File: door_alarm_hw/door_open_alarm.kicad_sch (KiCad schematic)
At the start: 60 parts, among them J1 TYPE-C 16PIN 2MD(073), Q1 BSS138PW,115, Q2 CJ2301 S1, Q3 CJ2301 S1, SW1 SW_Reed, U1 AP2114HA-3.3TRG1, U2 ESP32-S3-MINI-1

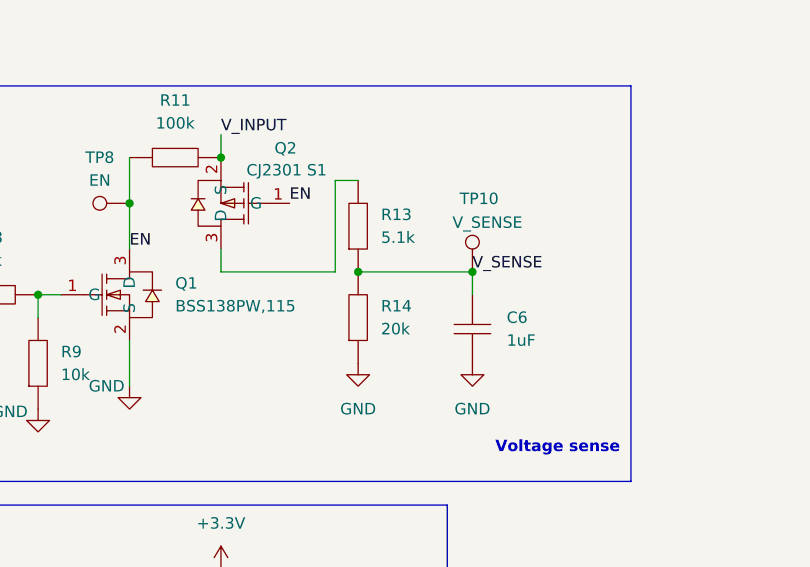
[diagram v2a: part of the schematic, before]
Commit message: Resistor mix up fix, label fix
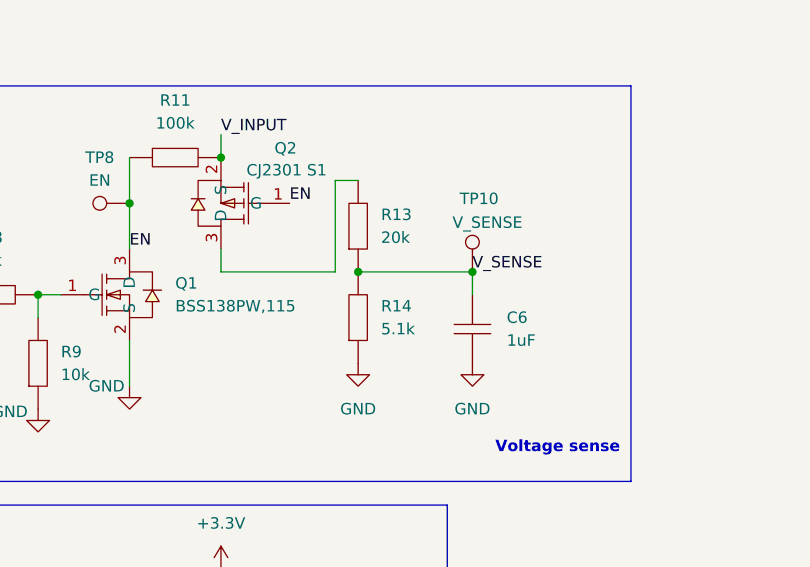
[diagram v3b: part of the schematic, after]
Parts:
- removed R13: 0805W8F5101T5E, pepy_sym_lib:[RES_SMD_0805_2012Metric], symbol pepy_sym_lib:[RES_SMD_0805_2012Metric]UNI-ROYAL(Uniroyal Elec) 0805W8F5101T5E
- removed R14: 0805W8J0203T5E, pepy_sym_lib:[RES_SMD_0805_2012Metric], symbol pepy_sym_lib:[RES_SMD_0805_2012Metric]UNI-ROYAL(Uniroyal Elec) 0805W8J0203T5E
- added R13: 0805W8J0203T5E, pepy_sym_lib:[RES_SMD_0805_2012Metric], symbol pepy_sym_lib:[RES_SMD_0805_2012Metric]UNI-ROYAL(Uniroyal Elec) 0805W8J0203T5E
- added R14: 0805W8F5101T5E, pepy_sym_lib:[RES_SMD_0805_2012Metric], symbol pepy_sym_lib:[RES_SMD_0805_2012Metric]UNI-ROYAL(Uniroyal Elec) 0805W8F5101T5E
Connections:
- net GND: now also R14.1
- net V_SENSE: now also R13.1, R14.2
- net at Q2.3 (D): now also R13.2
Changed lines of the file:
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@@
 	)
 	(junction
-		(at 111.76 172.72)
-		(diameter 0)
-		(color 0 0 0 0)
-	)
-	(junction
 		(at 96.52 228.6)
 		(diameter 0)
@@
 	)
 	(junction
+		(at 111.76 172.72)
+		(diameter 0)
+		(color 0 0 0 0)
+	)
+	(junction
 		(at 104.14 124.46)
 		(diameter 0)
@@
 	)
 	(symbol
-		(lib_id "pepy_sym_lib:[RES_SMD_0805_2012Metric]UNI-ROYAL(Uniroyal Elec) 0805W8F5101T5E")
-		(at 111.76 167.64 90)
-		(unit 1)
-		(exclude_from_sim no)
-		(in_bom yes)
-		(on_board yes)
-		(dnp no)
-		(fields_autoplaced yes)
-		(property "Reference" "R13"
-			(at 114.3 166.3699 90)
-			(effects
-				(font
-					(size 1.27 1.27)
-				)
-				(justify right)
-			)
-		)
-		(property "Value" "0805W8F5101T5E"
-			(at 108.966 167.64 0)
-			(effects
-				(font
-					(size 1.27 1.27)
-				)
-				(hide yes)
-			)
-		)
-		(property "Footprint" "pepy_sym_lib:[RES_SMD_0805_2012Metric]"
-			(at 116.84 167.386 0)
-			(effects
-				(font
-					(size 1.27 1.27)
-				)
-				(hide yes)
-			)
-		)
-		(property "Datasheet" "https://lcsc.com/product-detail/Chip-Resistor-Surface-Mount-UniOhm_5-1KR-5101-1_C27834.html"
-			(at 119.38 167.386 0)
-			(effects
-				(font
-					(size 1.27 1.27)
-				)
-				(hide yes)
-			)
-		)
-		(property "Description" "125mW Thick Film Resistors 150V ±100ppm/℃ ±1% 5.1kΩ 0805 Chip Resistor - Surface Mount ROHS"
-			(at 124.206 167.64 0)
-			(effects
-				(font
-					(size 1.27 1.27)
-				)
-				(hide yes)
-			)
-		)
-		(property "LCSC Part" "C27834"
-			(at 121.92 167.386 0)
-			(effects
-				(font
-					(size 1.27 1.27)
-				)
-				(hide yes)
-			)
-		)
-		(property "Nvalue" "5.1k"
-			(at 114.3 168.9099 90)
-			(effects
-				(font
-					(size 1.27 1.27)
-				)
-				(justify right)
-			)
-		)
-		(property "Manufacturer" "UNI-ROYAL(Uniroyal Elec)"
-			(at 126.746 167.132 0)
-			(effects
-				(font
-					(size 1.27 1.27)
-				)
-				(hide yes)
-			)
-		)
-		(property "Package" "0805"
-			(at 128.778 167.132 0)
-			(effects
-				(font
-					(size 1.27 1.27)
-				)
-				(hide yes)
-			)
-		)
-		(pin "2"
-		)
-		(pin "1"
-		)
-		(instances
-			(project "door_open_alarm"
-				(path "/a0bc7b41-b457-4d21-bf6e-3cc6c082f129"
-					(reference "R13")
-					(unit 1)
-				)
-			)
-		)
-	)
-	(symbol
 		(lib_id "Mechanical:Fiducial")
 		(at 83.82 250.19 0)
@@
 	)
 	(symbol
+		(lib_id "pepy_sym_lib:[RES_SMD_0805_2012Metric]UNI-ROYAL(Uniroyal Elec) 0805W8F5101T5E")
+		(at 111.76 177.8 90)
+		(unit 1)
+		(exclude_from_sim no)
+		(in_bom yes)
+		(on_board yes)
+		(dnp no)
+		(fields_autoplaced yes)
+		(property "Reference" "R14"
+			(at 114.3 176.5299 90)
+			(effects
+				(font
+					(size 1.27 1.27)
+				)
+				(justify right)
+			)
+		)
+		(property "Value" "0805W8F5101T5E"
+			(at 108.966 177.8 0)
+			(effects
+				(font
+					(size 1.27 1.27)
+				)
+				(hide yes)
+			)
+		)
+		(property "Footprint" "pepy_sym_lib:[RES_SMD_0805_2012Metric]"
+			(at 116.84 177.546 0)
+			(effects
+				(font
+					(size 1.27 1.27)
+				)
+				(hide yes)
+			)
+		)
+		(property "Datasheet" "https://lcsc.com/product-detail/Chip-Resistor-Surface-Mount-UniOhm_5-1KR-5101-1_C27834.html"
+			(at 119.38 177.546 0)
+			(effects
+				(font
+					(size 1.27 1.27)
+				)
+				(hide yes)
+			)
+		)
+		(property "Description" "125mW Thick Film Resistors 150V ±100ppm/℃ ±1% 5.1kΩ 0805 Chip Resistor - Surface Mount ROHS"
+			(at 124.206 177.8 0)
+			(effects
+				(font
+					(size 1.27 1.27)
+				)
+				(hide yes)
+			)
+		)
+		(property "LCSC Part" "C27834"
+			(at 121.92 177.546 0)
+			(effects
+				(font
+					(size 1.27 1.27)
+				)
+				(hide yes)
+			)
+		)
+		(property "Nvalue" "5.1k"
+			(at 114.3 179.0699 90)
+			(effects
+				(font
+					(size 1.27 1.27)
+				)
+				(justify right)
+			)
+		)
+		(property "Manufacturer" "UNI-ROYAL(Uniroyal Elec)"
+			(at 126.746 177.292 0)
+			(effects
+				(font
+					(size 1.27 1.27)
+				)
+				(hide yes)
+			)
+		)
+		(property "Package" "0805"
+			(at 128.778 177.292 0)
+			(effects
+				(font
+					(size 1.27 1.27)
+				)
+				(hide yes)
+			)
+		)
+		(pin "1"
+		)
+		(pin "2"
+		)
+		(instances
+			(project ""
+				(path "/a0bc7b41-b457-4d21-bf6e-3cc6c082f129"
+					(reference "R14")
+					(unit 1)
+				)
+			)
+		)
+	)
+	(symbol
 		(lib_id "pepy_sym_lib:[ESD_PROT]Nexperia IP4283CZ10-TBR,115")
 		(at 104.14 35.56 0)
@@
 	)
 	(symbol
-		(lib_id "pepy_sym_lib:[RES_SMD_0805_2012Metric]UNI-ROYAL(Uniroyal Elec) 0805W8J0203T5E")
-		(at 111.76 177.8 90)
-		(unit 1)
-		(exclude_from_sim no)
-		(in_bom yes)
-		(on_board yes)
-		(dnp no)
-		(fields_autoplaced yes)
-		(property "Reference" "R14"
-			(at 114.3 176.5299 90)
-			(effects
-				(font
-					(size 1.27 1.27)
-				)
-				(justify right)
-			)
-		)
-		(property "Value" "0805W8J0203T5E"
-			(at 108.966 177.8 0)
-			(effects
-				(font
-					(size 1.27 1.27)
-				)
-				(hide yes)
-			)
-		)
-		(property "Footprint" "pepy_sym_lib:[RES_SMD_0805_2012Metric]"
-			(at 116.84 177.546 0)
-			(effects
-				(font
-					(size 1.27 1.27)
-				)
-				(hide yes)
-			)
-		)
-		(property "Datasheet" "https://lcsc.com/product-detail/Chip-Resistor-Surface-Mount-UniOhm_5-1KR-5101-1_C27834.html"
-			(at 119.38 177.546 0)
-			(effects
-				(font
-					(size 1.27 1.27)
-				)
-				(hide yes)
-			)
-		)
-		(property "Description" "125mW Thick Film Resistors 150V ±100ppm/℃ ±5% 20kΩ 0805 Chip Resistor - Surface Mount ROHS"
-			(at 124.206 177.8 0)
-			(effects
-				(font
-					(size 1.27 1.27)
-				)
-				(hide yes)
-			)
-		)
-		(property "LCSC Part" "C25624"
-			(at 121.92 177.546 0)
-			(effects
-				(font
-					(size 1.27 1.27)
-				)
-				(hide yes)
-			)
-		)
-		(property "Nvalue" "20k"
-			(at 114.3 179.0699 90)
-			(effects
-				(font
-					(size 1.27 1.27)
-				)
-				(justify right)
-			)
-		)
-		(property "Manufacturer" "UNI-ROYAL(Uniroyal Elec)"
-			(at 126.746 177.292 0)
-			(effects
-				(font
-					(size 1.27 1.27)
-				)
-				(hide yes)
-			)
-		)
-		(property "Package" "0805"
-			(at 128.778 177.292 0)
-			(effects
-				(font
-					(size 1.27 1.27)
-				)
-				(hide yes)
-			)
-		)
-		(pin "2"
-		)
-		(pin "1"
-		)
-		(instances
-			(project "door_open_alarm"
-				(path "/a0bc7b41-b457-4d21-bf6e-3cc6c082f129"
-					(reference "R14")
-					(unit 1)
-				)
-			)
-		)
-	)
-	(symbol
 		(lib_id "Switch:SW_Reed")
 		(at 83.82 228.6 0)
@@
 					(unit 1)
 				)
+			)
+		)
+	)
+	(symbol
+		(lib_id "pepy_sym_lib:[RES_SMD_0805_2012Metric]UNI-ROYAL(Uniroyal Elec) 0805W8J0203T5E")
+		(at 111.76 167.64 90)
+		(unit 1)
+		(exclude_from_sim no)
+		(in_bom yes)
+		(on_board yes)
+		(dnp no)
+		(fields_autoplaced yes)
+		(property "Reference" "R13"
+			(at 114.3 166.3699 90)
+			(effects
+				(font
+					(size 1.27 1.27)
+				)
+				(justify right)
+			)
+		)
+		(property "Value" "0805W8J0203T5E"
+			(at 108.966 167.64 0)
+			(effects
+				(font
+					(size 1.27 1.27)
+				)
+				(hide yes)
+			)
+		)
+		(property "Footprint" "pepy_sym_lib:[RES_SMD_0805_2012Metric]"
+			(at 116.84 167.386 0)
+			(effects
+				(font
+					(size 1.27 1.27)
+				)
+				(hide yes)
+			)
+		)
+		(property "Datasheet" "https://lcsc.com/product-detail/Chip-Resistor-Surface-Mount-UniOhm_5-1KR-5101-1_C27834.html"
+			(at 119.38 167.386 0)
+			(effects
+				(font
+					(size 1.27 1.27)
+				)
+				(hide yes)
+			)
+		)
+		(property "Description" "125mW Thick Film Resistors 150V ±100ppm/℃ ±5% 20kΩ 0805 Chip Resistor - Surface Mount ROHS"
+			(at 124.206 167.64 0)
+			(effects
+				(font
+					(size 1.27 1.27)
+				)
+				(hide yes)
+			)
+		)
+		(property "LCSC Part" "C25624"
+			(at 121.92 167.386 0)
+			(effects
+				(font
+					(size 1.27 1.27)
+				)
+				(hide yes)
+			)
+		)
+		(property "Nvalue" "20k"
+			(at 114.3 168.9099 90)
+			(effects
+				(font
+					(size 1.27 1.27)
+				)
+				(justify right)
+			)
+		)
+		(property "Manufacturer" "UNI-ROYAL(Uniroyal Elec)"
+			(at 126.746 167.132 0)
+			(effects
+				(font
+					(size 1.27 1.27)
+				)
+				(hide yes)
+			)
+		)
+		(property "Package" "0805"
+			(at 128.778 167.132 0)
+			(effects
+				(font
+					(size 1.27 1.27)
+				)
+				(hide yes)
+			)
+		)
+		(pin "1"
+		)
+		(pin "2"
+		)
+		(instances
+			(project ""
+				(path "/a0bc7b41-b457-4d21-bf6e-3cc6c082f129"
+					(reference "R13")
+					(unit 1)
+				)
